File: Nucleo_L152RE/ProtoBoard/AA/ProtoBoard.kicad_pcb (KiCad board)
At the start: 2 copper layers, 70.5 x 81.3 mm, 110 parts, among them CON1 USB-MICRO-B, J1 EXT1, J2 EXT2, J3 EXTPower, P1 Power, P10 OW2_A, P11 GND1, P12 I2C1_B, P13 I2C2_B, P14 SW_1_6, P15 WS1, P16 WS2, P17 MS2, P18 WS3, P19 WS4, P2 VinPower, P20 GND2, P22 MS3, P23 OW3_A, P24 OW4_A, P25 MS4, P28 RGB1, P29 Ant, P3 USART2, P4 SWD Header, P5 USART1, P6 MS1, P7 I2C1_A, P8 I2C2_A, P9 OW1_A, Q1 SI2323DS, SW1 MomentarySwitch, U2 Nucleo-L152RE-CN7, U3 Nucleo-L152RE-CN10, U5 MT3329_GPS, U6 S25FL127S, U7 RFM69HW

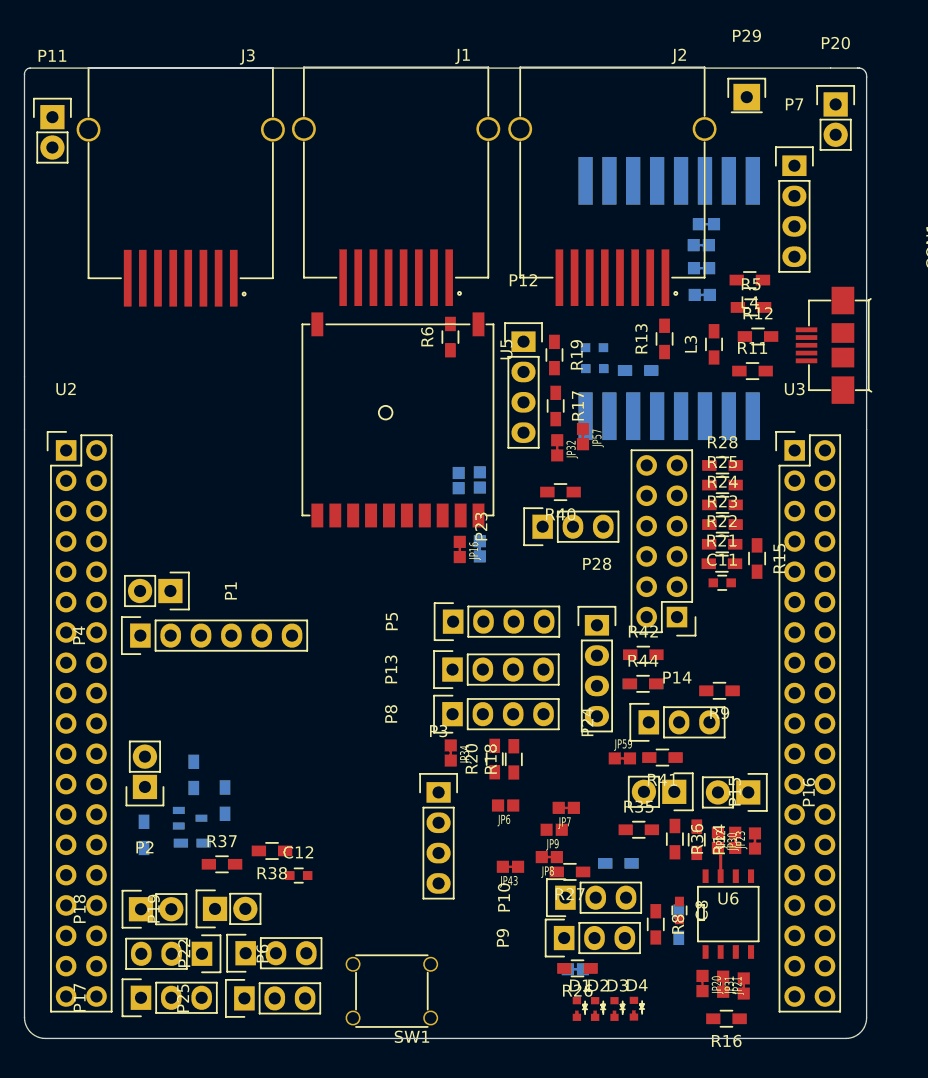
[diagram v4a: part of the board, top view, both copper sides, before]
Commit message: performing more routing of the board.  This board is quickly becoming complicated with all of the headers to navigate around.
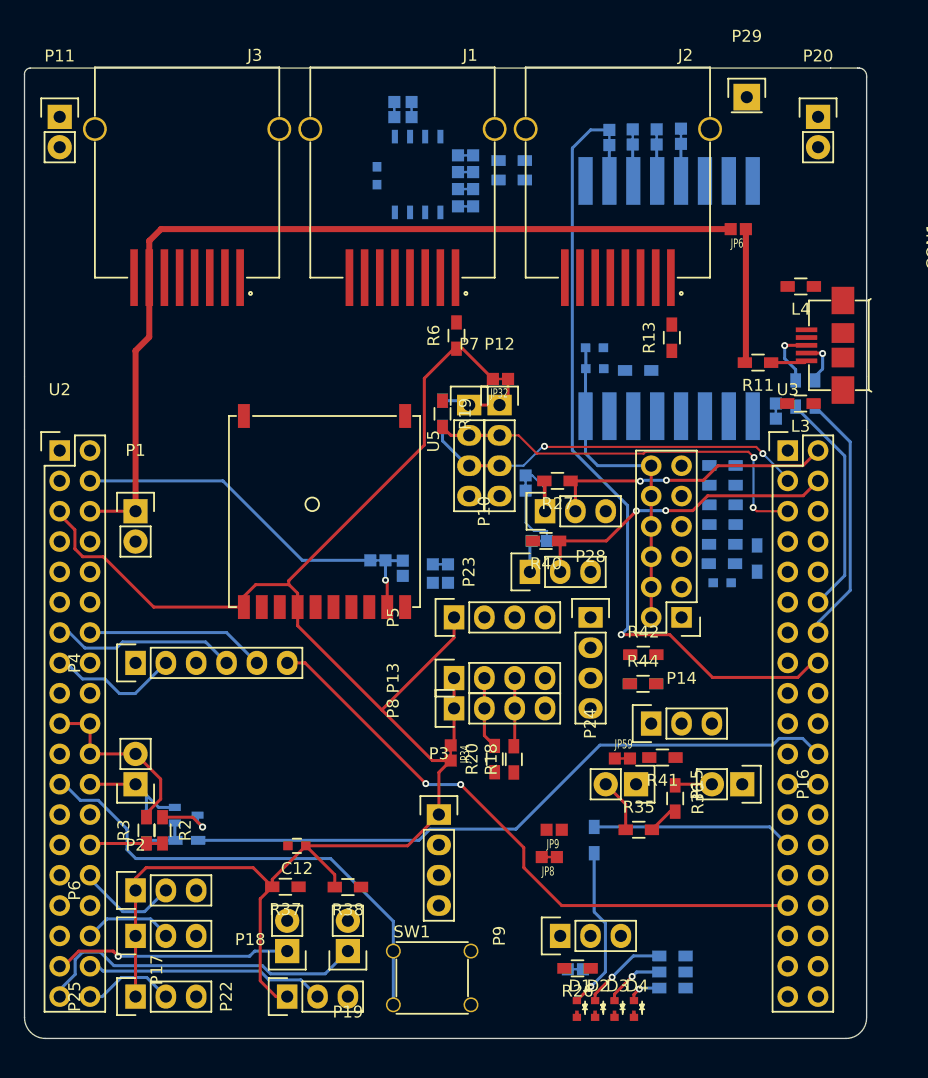
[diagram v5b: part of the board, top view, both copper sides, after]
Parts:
- C11, C8, JP16, JP20, JP21, JP22, JP23, JP30, JP31, JP43, JP57, JP7, R12, R14, R15, R16, R17, R21, R22, R23, R24, R25, R28, R5, R8, R9, U6: moved to B.Cu
- R2, R3: moved to F.Cu
- moved JP21 77.7 mm to (153.9, 51.5), turned to 270 degrees
- moved JP20 77.6 mm to (152.5, 51.5), turned to 270 degrees
- moved R16 74.1 mm to (162.3, 55.7), turned to 0 degrees
- moved JP31 73.3 mm to (158.4, 55.3), turned to 0 degrees
- moved U6 67.2 mm to (154.4, 56.9)
- moved C8 66.5 mm to (151.0, 57.0), turned to 90 degrees
- moved JP30 59.8 mm to (158.4, 56.7), turned to 0 degrees
- moved JP22 59.0 mm to (158.4, 58.1), turned to 180 degrees
- moved JP23 58.4 mm to (158.4, 59.6), turned to 180 degrees
- moved R14 57.4 mm to (162.3, 57.4), turned to 0 degrees
- moved JP6 52.0 mm to (181.3, 61.5)
- moved JP7 37.6 mm to (184.4, 76.7), turned to 90 degrees
- moved P7 33.8 mm to (158.8, 76.2)
- moved R27 32.8 mm to (166.1, 82.5)
- moved P10 32.4 mm to (165.1, 85.1)
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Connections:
- P3 pad 3: (no net) -> /USART2_RX
- U3 pad 37: (no net) -> /USART2_RX
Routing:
- net +3V3: track 0.00 -> 182.4 mm
- net /E5V: track 0.00 -> 76.0 mm
- net /SPI2_NSS: track 0.00 -> 65.1 mm, vias 0 -> 1
- net /VIN_Trig: track 0.00 -> 56.0 mm
- net /SWO: track 0.00 -> 51.3 mm, vias 0 -> 2
- net /StatusButton1: track 0.00 -> 40.7 mm
- net /I2C_SDA1: track 0.00 -> 34.5 mm, vias 0 -> 2
- net /I2C_SCL1: track 0.00 -> 33.7 mm, vias 0 -> 2
- net /WS4: track 0.00 -> 28.3 mm
- net /OneWireBus3: track 0.00 -> 26.4 mm, vias 0 -> 2
- net /GPS_RX: track 0.00 -> 26.2 mm
- net /OneWireBus2: track 0.00 -> 24.5 mm, vias 0 -> 2
- net /USB_DM: track 0.00 -> 21.3 mm
- net /MotionSense3: track 0.00 -> 20.1 mm
- net /WS3: track 0.00 -> 19.9 mm, vias 0 -> 1
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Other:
- net class Default: via_dia 0.6 -> 0.5842; via_drill 0.4 -> 0.381
- net class Power added: clearance 0.2, trace_width 2.54, via_dia 0.5842, via_drill 0.381
- rule trace_min: 0.2 -> 0.1778

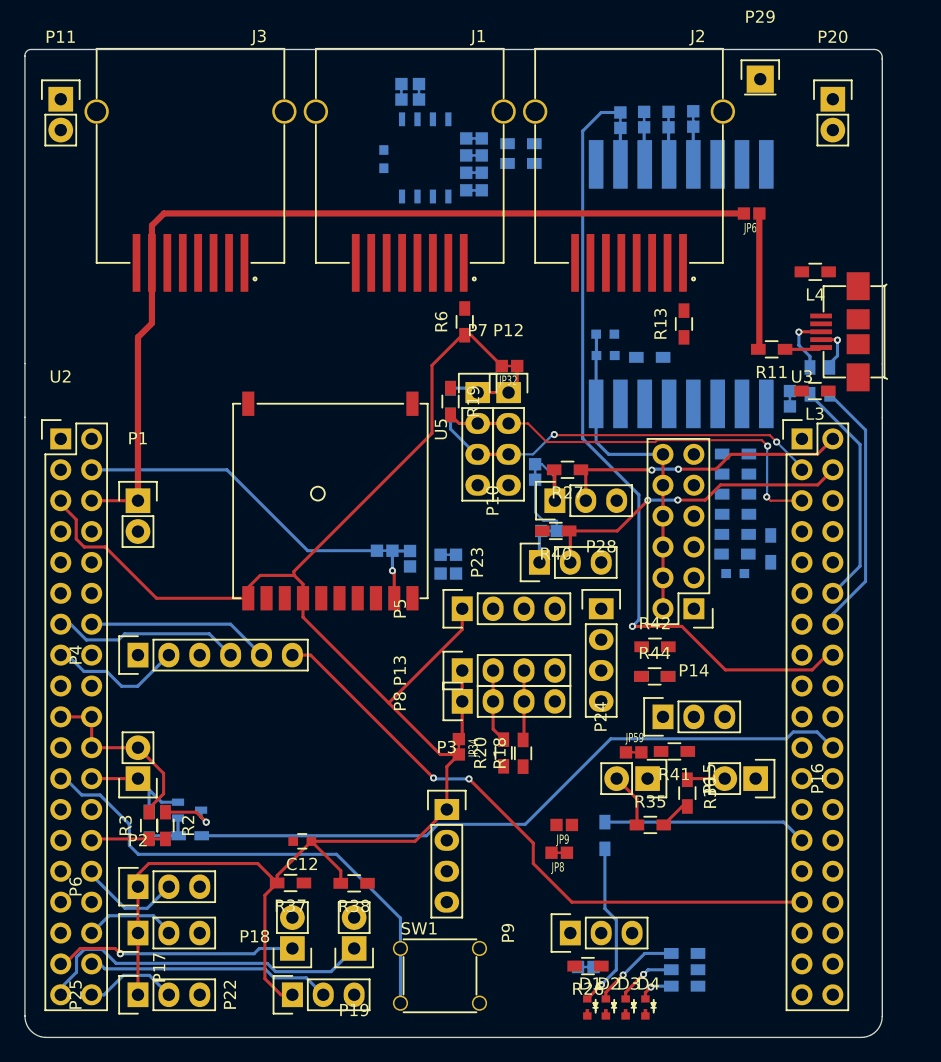
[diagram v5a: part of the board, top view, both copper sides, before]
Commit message: All signals routed, now the only remaining thing is ground signals and/or ground planes.
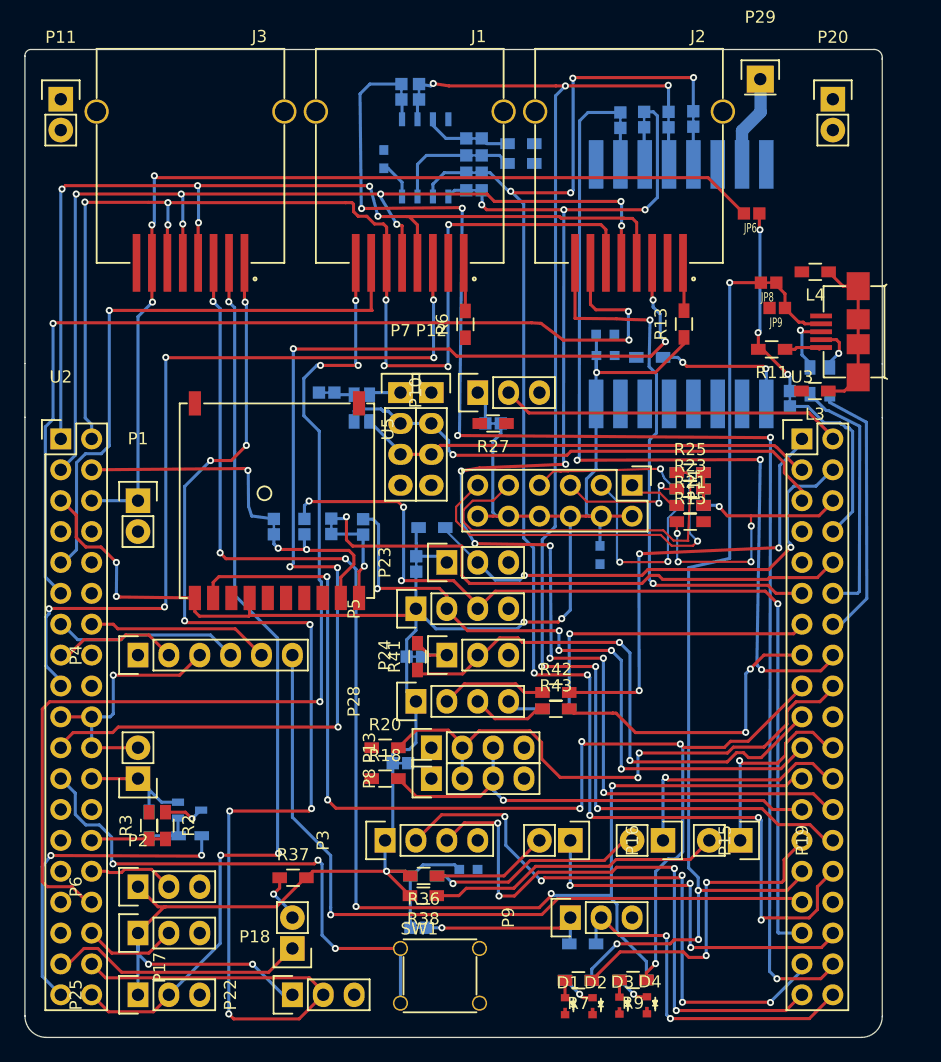
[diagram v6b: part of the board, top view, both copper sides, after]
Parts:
- C12, JP32, JP34, JP59, R19, R26, R35, R40, R44: moved to B.Cu
- R15, R21, R23, R25, R43, R7, R9: moved to F.Cu
- moved JP8 50.0 mm to (182.7, 67.2)
- moved JP9 46.0 mm to (183.4, 69.2)
- moved P19 33.0 mm to (180.3, 113.0), turned to 270 degrees
- moved R36 22.7 mm to (154.3, 116.0), turned to 180 degrees
- moved R41 22.5 mm to (153.8, 97.9), turned to 90 degrees
- moved JP59 19.7 mm to (153.5, 97.9)
- moved R35 19.1 mm to (154.3, 116.0), turned to 180 degrees
- moved P24 18.5 mm to (156.2, 97.8)
- moved P28 17.0 mm to (153.7, 101.6), turned to 90 degrees
- moved P16 16.1 mm to (166.4, 113.0)
- moved JP32 15.2 mm to (146.3, 76.2)
- moved JP41 14.2 mm to (153.8, 120.2), turned to 180 degrees
- moved C12 13.9 mm to (158.0, 115.4), turned to 0 degrees
- moved R7 12.1 mm to (167.0, 124.5), turned to 180 degrees
- moved R18 11.5 mm to (151.1, 108.0), turned to 0 degrees
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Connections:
- U2 pad 37: /WS4 -> /VIN_Trig
- U3 pad 22: /VIN_Trig -> /WS4
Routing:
- net /StatusLed4: track 0.00 -> 118.3 mm, vias 0 -> 6
- net /SPI2_SCK: track 0.00 -> 117.9 mm, vias 0 -> 9
- net /FLASH_nCS: track 0.00 -> 116.0 mm, vias 0 -> 5
- net /SPI2_MOSI: track 0.00 -> 110.5 mm, vias 0 -> 10
- net /SPI2_MISO: track 0.00 -> 108.0 mm, vias 0 -> 6
- net /StatusLed3: track 0.00 -> 97.4 mm, vias 0 -> 6
- net /EXT2_SPI_CS: track 0.00 -> 97.1 mm, vias 0 -> 6
- net /EXT_SPI_MISO: track 0.00 -> 95.1 mm, vias 0 -> 7
- net /MotionSense3: track 20.1 -> 110.8 mm, vias 0 -> 8
- net /EXT_SPI_MOSI: track 0.00 -> 85.5 mm, vias 0 -> 7
- net /EXT_SPI_CLK: track 0.00 -> 84.1 mm, vias 0 -> 5
- net /EXT1_GPIO: track 0.00 -> 82.7 mm, vias 0 -> 4
- net /EXT2_ADC: track 0.00 -> 80.0 mm, vias 0 -> 3
- net /StatusLed2: track 0.00 -> 79.8 mm, vias 0 -> 4
- net /USART1_RX: track 0.00 -> 77.9 mm, vias 0 -> 4
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
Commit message: All pads now connected.
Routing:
- net GND: track 22.1 -> 518.9 mm, vias 1 -> 33
- net +3V3: track 204.4 -> 265.9 mm, vias 8 -> 14
- net Net-(JP34-Pad2): track 0.00 -> 13.8 mm, vias 0 -> 1
- net Net-(JP43-Pad1): track 2.80 -> 5.41 mm
- net /OneWireBus2: track 28.4 -> 31.0 mm
- net Net-(JP32-Pad2): track 5.58 -> 8.12 mm
- net /SWBus: track 30.5 -> 31.8 mm
- net /StatusLed3: track 97.4 -> 98.1 mm

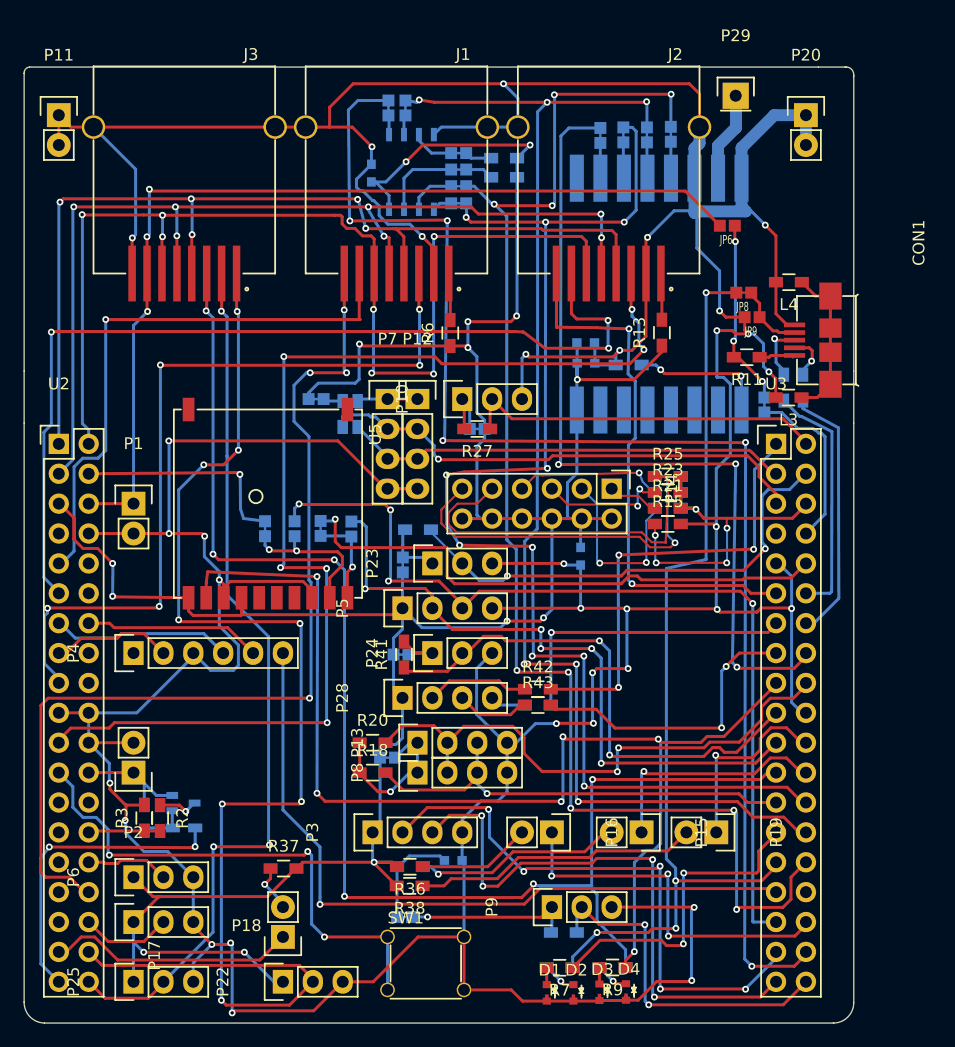
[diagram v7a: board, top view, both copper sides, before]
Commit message: About to modify Solder Bridges to be a smaller 0402 package rather than the custom one which generates DRC errors.
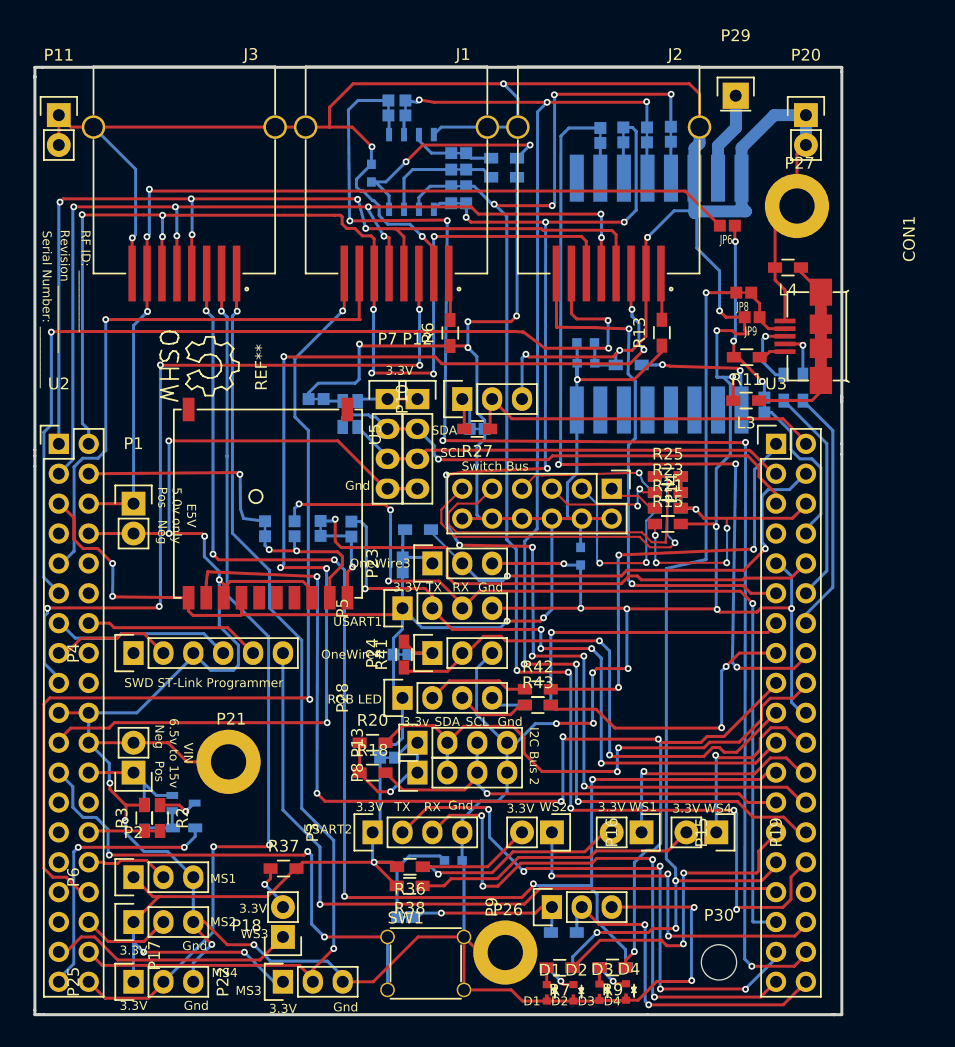
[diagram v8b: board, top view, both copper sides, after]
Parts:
- added P21: Hole, nucleo:plat_hole_4_20, F.Cu at (138.9, 107.1)
- added P26: Hole, nucleo:plat_hole_4_20, F.Cu at (162.4, 123.3)
- added P27: Hole, nucleo:plat_hole_4_20, F.Cu at (187.2, 59.8)
- added P30: Hole, Mounting_Holes:MountingHole_3mm, F.Cu at (180.6, 124.1)
- added REF**: Symbol_OSHW-Logo_SilkScreen, Symbols:Symbol_OSHW-Logo_SilkScreen, F.Cu at (137.3, 73.4)
- moved L3 3.62 mm to (182.9, 76.3)
- moved L4 1.25 mm to (186.4, 65.0)
- moved CON1 0.88 mm to (189.2, 70.9)
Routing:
- net /MotionSense3: track 110.8 -> 84.9 mm, vias 8 -> 2
- net GND: track 518.9 -> 528.7 mm, vias 33 -> 30
- net GNDPWR: track 13.3 -> 16.8 mm
- net /VIN_Trig: track 26.4 -> 23.2 mm
- net /EXT1_GPIO: track 82.7 -> 80.3 mm, vias 4 -> 2
- net /USB_DP: track 21.2 -> 19.0 mm
- net Net-(CON1-Pad3): track 5.14 -> 6.55 mm
- net /U5V: track 14.9 -> 13.8 mm
- net Net-(CON1-Pad1): track 3.23 -> 2.35 mm
- net Net-(CON1-Pad4): track 5.90 -> 5.10 mm
- net /USB_DM: track 22.3 -> 21.6 mm
- net Net-(CON1-Pad2): track 4.30 -> 4.83 mm
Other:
- board size 70.5 x 81.3 mm -> 68.6 x 80.5 mm
- rule via_min_drill: 0.3 -> 0.381
- rule via_min_size: 0.4 -> 0.5842
- board text added: "3.3V"
- board text added: "3.3v"
- board text added: "D1"
- board text added: "D2"
- board text added: "D3"
- board text added: "D4"
- board text added: "Dustin Reynolds"
- board text added: "E5V 5.0v only Pos Neg"
- board text added: "Extension 1"
- board text added: "Extension 2"
- board text added: "Gnd"
- board text added: "I2C Bus 2"
- board text added: "MS1"
- board text added: "MS2"
- board text added: "MS3"
- board text added: "MS4"
- board text added: "MT3329 GPS Module"
- board text added: "OneWire3"
- board text added: "OneWire4"
- board text added: "PowerExt"
- board text added: "RF ID: __________"
- board text added: "RFM69HW Wireless Module"
- board text added: "RGB LED"
- board text added: "RX"
- board text added: "Revision ___________"
- board text added: "SCL"
- board text added: "SDA"
- board text added: "STM32 Sensor Shield"
- board text added: "SWD ST-Link Programmer"
- board text added: "Serial Number: __________"
- board text added: "Switch Bus"
- board text added: "TX"
- board text added: "USART1"
- board text added: "USART2"
- board text added: "VIN 6.5v to 15v Neg Pos"
- board text added: "WS1"
- board text added: "WS2"
- board text added: "WS3"
- board text added: "WS4"
